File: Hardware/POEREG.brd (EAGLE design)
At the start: 30.5 x 33 mm, 9 parts, among them J1 SJCN

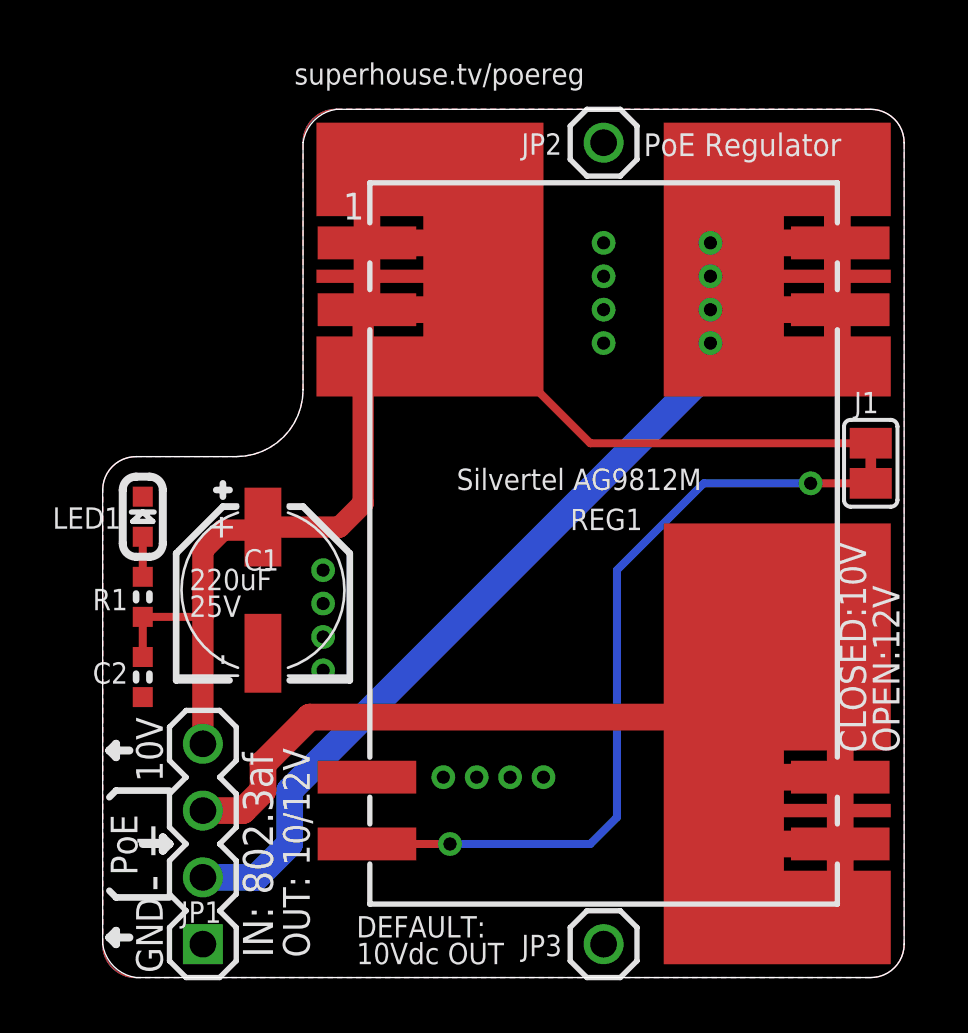
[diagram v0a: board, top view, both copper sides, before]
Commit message: Replace Silvertel module with AG9912LP.
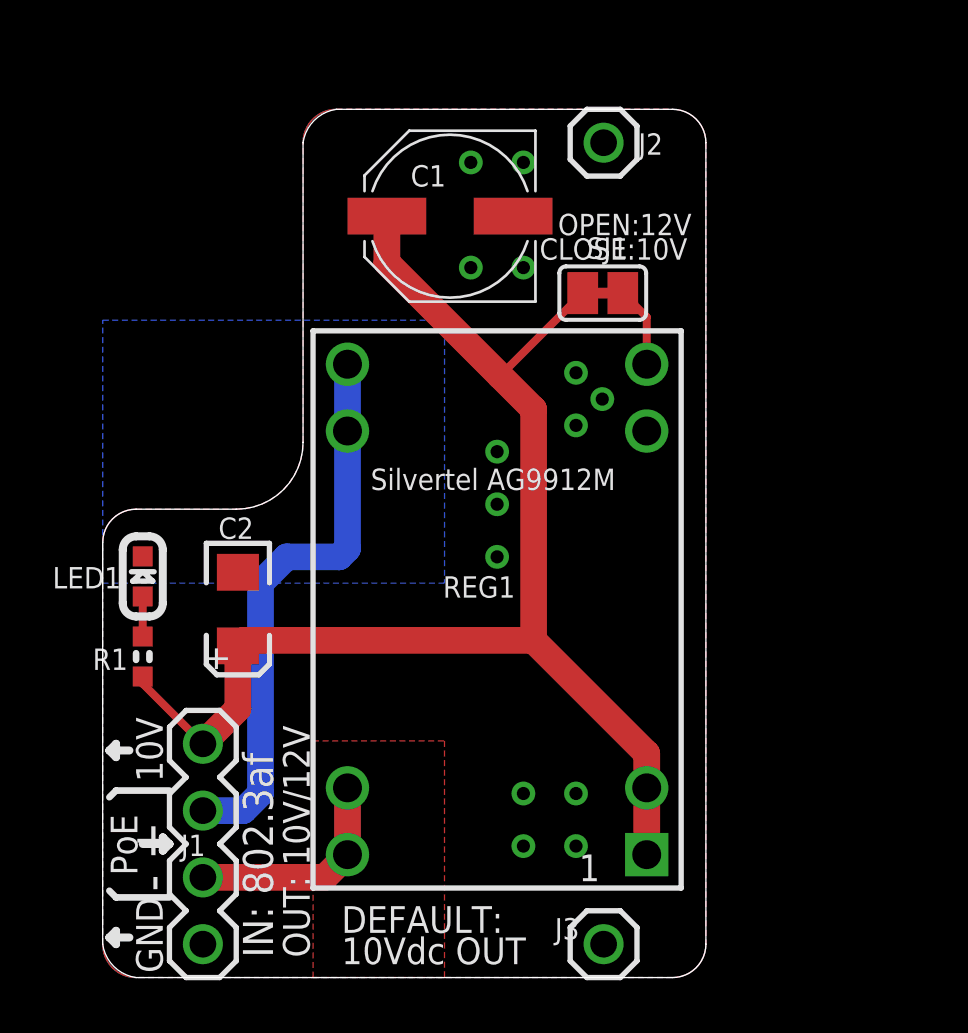
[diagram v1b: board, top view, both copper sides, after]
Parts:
- removed JP1: PoE Header, freetronics:1X04
- removed JP2, JP3: (no value), freetronics:1X01
- added J2, J3: M01-PLAIN, SuperHouse-Connectors:1X01
- added SJ1: SJC-NORMAL, SuperHouse-Jumpers:SJC
- C1: value 220uF 25V -> 100uF 25V; device rcl:PANASONIC_D -> SuperHouse-DiscreteSemi:PANASONIC_D
- C2: value 100nF 0603 -> 10uF 1206; device freetronics-master-v1.1:0603 -> SuperHouse-DiscreteSemi:EIA3216
- J1: value SJCN -> PoE Header; device freetronics-jon:SJC -> SuperHouse-Connectors:1X04
- LED1: device freetronics:LED-0603 -> SuperHouse-LEDs:LED-0603
- R1: value 2K2 -> 4K7; device freetronics:0603 -> SuperHouse-DiscreteSemi:R0603
- REG1: value AG9800 -> AG9912LP; device freetronics-jon:AG9800 -> SuperHouse-Regulators:AG9900LP
- moved J1 29.2 mm to (3.81, 5.08), turned to 90 degrees
- moved C1 15.9 mm to (13.2, 29.0), turned to 180 degrees
- moved REG1 4.76 mm to (15.0, 14.0), turned to 180 degrees
- moved C2 4.45 mm to (5.14, 14.0)
- moved LED1 2.27 mm to (1.52, 15.3)
- moved R1 2.27 mm to (1.52, 12.2)
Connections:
- net +VDC: now also C2.A, J1.4, SJ1.1; no longer C2.1, J1.1, JP1.4
- net GND: now also C2.C, J1.1, J3.1; no longer C2.2, JP1.1, JP3.1
- net N$1: now also SJ1.2; no longer J1.2
- net VIN+: now also J1.3; no longer JP1.3
- net VIN-: now also J1.2; no longer JP1.2
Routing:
- net VIN-: track 54.2 -> 8.40 mm, vias 4 -> 0
- net N$1: track 30.3 -> 3.08 mm, vias 2 -> 0
- net VIN+: track 39.7 -> 21.3 mm
- net +VDC: track 58.6 -> 51.9 mm
- added copper zone on layer 16, net VIN+
- added copper zone on layer 1, net VIN-
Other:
- board size 30.5 x 33 mm -> 22.9 x 33 mm
- board text added: "(c) 2013-2021 Freetronics Pty Ltd"
- board text added: "802.3af PoE Regulator"
- board text added: "CLOSE:10V"
- board text added: "OUT: 10V/12V"
- board text added: "SKU: POEREG v3.0"
- board text added: "Silvertel AG9912M"
- board text added: "freetronics"
- board text added: "tron.cc/poereg"
- board text added: "www.freetronics.com"
- board text removed: "(c) 2018 SuperHouse Automation"
- board text removed: "-"
- board text removed: "220uF"
- board text removed: "25V"
- board text removed: "CLOSED:10V"
- board text removed: "OUT: 10/12V"
- board text removed: "PoE Regulator"
- board text removed: "SKU: POEREG v2.1"
- board text removed: "Silvertel AG9812M"
- board text removed: "superhouse.tv/poereg"
